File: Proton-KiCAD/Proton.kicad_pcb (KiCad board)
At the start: 4 copper layers, 92.6 x 57.2 mm, 85 parts, among them J1 USB_C_Receptacle_USB2.0_14P, J2 KEYPAD, J3 AudioJack3, J4 SPEAKER_OUT, J5 OLED SPI, J6 ROTARY ENCODER, J7 OLED, J8 SI4703, J9 Conn_01x03_Pin, SW1 BOOTSEL, SW2 RESET, U1 W25Q128JVS, U2 USBLC6-2P6, U3 NCP1117-3.3_SOT223, U4 RP2350_80QFN, U5 TL072, U6 LM386, Y1 ABM8-272-T3

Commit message: ready for final check
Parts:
- added C34: 22uF, Capacitor_SMD:C_0805_2012Metric, B.Cu at (181.5, 56.0)
- added C35: 22uF, Capacitor_SMD:C_0805_2012Metric, B.Cu at (175.2, 56.5)
- added J10: BATTERY IN, Connector_PinHeader_2.54mm:PinHeader_1x02_P2.54mm_Vertical, F.Cu at (180.2, 46.0)
- added J11: FRONT_BUTTON_1, Connector_PinHeader_2.54mm:PinHeader_1x02_P2.54mm_Vertical, F.Cu at (131.8, 64.7)
- added J12: FRONT_BUTTON_2, Connector_PinHeader_2.54mm:PinHeader_1x02_P2.54mm_Vertical, F.Cu at (127.5, 64.7)
- added R31: 1k, Resistor_SMD:R_0402_1005Metric, F.Cu at (135.2, 69.5)
- added R32: 1k, Resistor_SMD:R_0402_1005Metric, F.Cu at (135.2, 67.2)
- added U7: AMS1117-5.0, Package_TO_SOT_SMD:SOT-223-3_TabPin2, B.Cu at (178.8, 50.8)
- C31: moved to B.Cu
- moved C31 5.50 mm to (189.0, 46.0)
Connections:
- U4 pad 11: /GPIO12 -> FRONT_BUTTON_1
- U4 pad 12: /GPIO13 -> FRONT_BUTTON_2
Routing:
- net +5V: track 25.9 -> 41.9 mm, vias 1 -> 2
- net Net-(J10-Pin_1): track 0.00 -> 14.1 mm
- net Net-(J12-Pin_1): track 0.00 -> 9.22 mm
- net Net-(C31-Pad2): track 9.95 -> 15.5 mm
- net FRONT_BUTTON_1: track 0.00 -> 4.96 mm
- net FRONT_BUTTON_2: track 0.00 -> 4.48 mm
- net Net-(J11-Pin_1): track 0.00 -> 4.04 mm
- net Net-(J4-Pin_1): track 6.58 -> 5.83 mm
- net GND: vias 111 -> 130

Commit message: Finished
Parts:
- added J14: DEBUGGER, Connector_PinHeader_2.54mm:PinHeader_1x03_P2.54mm_Vertical, F.Cu at (152.4, 79.5)
- C29: value 0.05 -> 0.05uF
- C3, C5, C6: moved to F.Cu
- C31: value 250uF -> 200uF; footprint Capacitor_THT:CP_Radial_D10.0mm_P5.00mm -> Capacitor_SMD:CP_Elec_6.3x4.5; moved to F.Cu
- J3: value AudioJack3 -> SJ-43514; footprint Connector_Audio:Jack_3.5mm_CUI_SJ-3523-SMT_Horizontal -> Custom_footprints:CUI_SJ-43514
- moved C3 9.34 mm to (145.5, 52.5), turned to 0 degrees
- moved U1 7.32 mm to (141.2, 56.0)
- moved L1 4.63 mm to (148.2, 59.2)
- moved C5 3.62 mm to (148.0, 62.2), turned to 0 degrees
- moved J4 3.10 mm to (184.0, 40.2), turned to 0 degrees
- moved R6 2.93 mm to (148.8, 51.5)
- moved C29 2.50 mm to (177.5, 53.5)
- moved R27 2.49 mm to (177.5, 51.0)
- moved C6 2.06 mm to (148.0, 61.0), turned to 0 degrees
- moved C31 1.27 mm to (190.2, 46.2)
- moved R9 1.00 mm to (146.5, 60.0)
- moved J3 0.69 mm to (200.9, 43.2), turned to -90 degrees
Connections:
- C29 pad 1: GND -> Net-(C29-Pad1)
- C31 pad 2: Net-(C31-Pad2) -> Net-(C29-Pad2)
- R15 pad 1: Net-(J3-PadT) -> Net-(J3-Pad2)
- R27 pad 1: Net-(C31-Pad2) -> Net-(C29-Pad1)
- R27 pad 2: Net-(C29-Pad2) -> GND
- U6 pad 5: Net-(C31-Pad2) -> Net-(C29-Pad2)
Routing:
- net Net-(C29-Pad2): track 1.50 -> 17.4 mm
- net Net-(C31-Pad2): track 15.5 -> 0.00 mm
- net /FLASH_SS: track 13.3 -> 28.0 mm
- net /QSPI_SD0: track 21.8 -> 8.85 mm
- net /SWD: track 0.00 -> 11.7 mm
- net /SWCLK: track 0.00 -> 9.65 mm
- net Net-(J3-Pad2): track 0.00 -> 8.34 mm, vias 0 -> 1
- net /QSPI_SCLK: track 14.6 -> 7.88 mm
- net Net-(J3-PadT): track 4.80 -> 0.00 mm, vias 1 -> 0
- net /QSPI_SD1: track 9.07 -> 13.0 mm
- net /~{USB_BOOT}: track 16.2 -> 13.1 mm
- net /QSPI_SD2: track 7.81 -> 10.1 mm
- net UART_RX: track 26.5 -> 28.5 mm
- net UART_TX: track 23.8 -> 25.7 mm
- net Net-(J4-Pin_1): track 5.83 -> 7.41 mm
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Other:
- board size 92.6 x 57.2 mm -> 92.8 x 57.2 mm
- board text added: "+3.3V"
- board text added: "- TEAM FLYING MACHINE"
- board text added: "FB_1"
- board text added: "FB_2"
- board text added: "GND"
- board text added: "ROTARY ENCODER"
- board text added: "RX"
- board text added: "SPKR"
- board text added: "SWCLK"
- board text added: "SWD"
- board text added: "Si4703"
- board text added: "TX"
- board text added: "{dblquote}SHABANG!{dblquote}"

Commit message: fixed audio section
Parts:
- added C27: 0.1uF, Capacitor_SMD:C_0402_1005Metric, F.Cu at (204.5, 50.1)
- added R33: 1k, Resistor_SMD:R_0402_1005Metric, F.Cu at (188.5, 65.1)
- added R34: 100k, Resistor_SMD:R_0402_1005Metric, F.Cu at (206.2, 54.6)
- turned R26 to 90 degrees
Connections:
- C22 pad 2: GND -> VGND
- C23 pad 1: GND -> VGND
- C23 pad 2: Net-(U5C-V-) -> GND
- C24 pad 2: GND -> VGND
- C30 pad 2: RF_AUDIO -> Net-(C30-Pad2)
- J3 pad 2: Net-(J3-Pad2) -> Net-(C27-Pad1)
- R15 pad 1: Net-(J3-Pad2) -> Net-(C27-Pad2)
- R26 pad 2: GND -> VGND
- R28 pad 2: RF_AUDIO -> Net-(C30-Pad2)
- R29 pad 1: RF_AUDIO -> Net-(C30-Pad2)
- U5 pad 4: Net-(U5C-V-) -> GND
- U6 pad 4: Net-(U6-GND) -> GND
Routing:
- net VGND: track 0.00 -> 44.9 mm, vias 0 -> 5
- net Net-(J3-Pad2): track 8.34 -> 0.00 mm, vias 1 -> 0
- net RF_AUDIO: track 45.7 -> 39.4 mm
- net Net-(C30-Pad2): track 0.00 -> 5.59 mm
- net Net-(C27-Pad2): track 0.00 -> 5.18 mm, vias 0 -> 1
- net Net-(C27-Pad1): track 0.00 -> 3.99 mm
- net Net-(U6-GND): track 3.81 -> 0.00 mm
- net GND: track 6.44 -> 9.70 mm, vias 131 -> 126
- net Net-(U5C-V-): track 3.25 -> 0.00 mm

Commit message: BOM CHANGES
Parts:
- removed the C27 at (174.5, 62.0)
- removed C28: 47uF, Capacitor_SMD:C_0805_2012Metric
- C27: value 0.1uF -> 22nF
- R15, R21: value 1k -> 2k
- R25: value 4k -> 9k
- R34: value 100k -> 2k
- moved C27 16.2 mm to (189.9, 57.1), turned to 0 degrees
- moved R34 15.9 mm to (190.4, 55.9), turned to 0 degrees
- moved C26 1.79 mm to (188.1, 55.9)
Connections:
- C26 pad 1: Net-(U5A--) -> Net-(C26-Pad1)
- C27 pad 1: Net-(C27-Pad1) -> Net-(C26-Pad1)
- C27 pad 2: Net-(C27-Pad2) -> VGND
- J3 pad 2: Net-(C27-Pad1) -> Net-(J3-Pad2)
- R15 pad 1: Net-(C27-Pad2) -> Net-(J3-Pad2)
- R34 pad 1: Net-(C27-Pad2) -> Net-(C26-Pad1)
- R34 pad 2: VGND -> Net-(U5A--)
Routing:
- net Net-(J3-Pad2): track 0.00 -> 8.54 mm
- net Net-(C27-Pad2): track 5.18 -> 0.00 mm, vias 1 -> 0
- net Net-(C27-Pad1): track 3.99 -> 0.00 mm
- net +5V: track 41.9 -> 37.9 mm
- net Net-(C26-Pad1): track 0.00 -> 2.76 mm
- net VGND: track 44.9 -> 45.8 mm
- net GND: vias 126 -> 124
- net /VREG_LX: vias 1 -> 0

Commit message: saving
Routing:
- net VGND: track 45.8 -> 44.9 mm
- net GND: vias 124 -> 134
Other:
- board text added: "- THE FLYING MACHINE"
- board text removed: "- TEAM FLYING MACHINE"
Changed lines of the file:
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@@
 		)
 	)
-	(gr_text "- TEAM FLYING MACHINE\n"
+	(gr_text "- THE FLYING MACHINE\n"
 		(at 191 82.75 0)
 		(layer "F.SilkS")
@@
 	)
 	(via
-		(at 172.5 64)
-		(size 0.6)
-		(drill 0.3)
-		(layers "F.Cu" "B.Cu")
-		(free yes)
-		(net 1)
-	)
-	(via
 		(at 185 50.25)
 		(size 0.6)
@@
 	)
 	(via
-		(at 172.5 63)
-		(size 0.6)
-		(drill 0.3)
-		(layers "F.Cu" "B.Cu")
-		(free yes)
-		(net 1)
-	)
-	(via
 		(at 174.5 38.5)
 		(size 0.6)
@@
 	)
 	(via
-		(at 174 65)
-		(size 0.6)
-		(drill 0.3)
-		(layers "F.Cu" "B.Cu")
-		(free yes)
-		(net 1)
-	)
-	(via
-		(at 176 64.5)
+		(at 175.5 60.65)
 		(size 0.6)
 		(drill 0.3)
@@
 	(via
 		(at 131 82.5)
+		(size 0.6)
+		(drill 0.3)
+		(layers "F.Cu" "B.Cu")
+		(free yes)
+		(net 1)
+	)
+	(via
+		(at 187.25 61.4)
 		(size 0.6)
 		(drill 0.3)
@@
 	)
 	(via
+		(at 197.010702 42.64261)
+		(size 0.6)
+		(drill 0.3)
+		(layers "F.Cu" "B.Cu")
+		(free yes)
+		(net 1)
+	)
+	(via
+		(at 176.25 59.9)
+		(size 0.6)
+		(drill 0.3)
+		(layers "F.Cu" "B.Cu")
+		(free yes)
+		(net 1)
+	)
+	(via
 		(at 171.5 42)
 		(size 0.6)
@@
 	(via
 		(at 169 55.5)
-		(size 0.6)
-		(drill 0.3)
-		(layers "F.Cu" "B.Cu")
-		(free yes)
-		(net 1)
-	)
-	(via
-		(at 172.5 62)
 		(size 0.6)
 		(drill 0.3)
@@
 	)
 	(via
+		(at 196.793598 38.662382)
+		(size 0.6)
+		(drill 0.3)
+		(layers "F.Cu" "B.Cu")
+		(free yes)
+		(net 1)
+	)
+	(via
 		(at 129 81.5)
 		(size 0.6)
@@
 	(via
 		(at 171.5 58)
+		(size 0.6)
+		(drill 0.3)
+		(layers "F.Cu" "B.Cu")
+		(free yes)
+		(net 1)
+	)
+	(via
+		(at 174 60.65)
 		(size 0.6)
 		(drill 0.3)
@@
 	)
 	(via
+		(at 197.851977 42.335047)
+		(size 0.6)
+		(drill 0.3)
+		(layers "F.Cu" "B.Cu")
+		(free yes)
+		(net 1)
+	)
+	(via
 		(at 200 51.5)
 		(size 0.6)
@@
 	)
 	(via
+		(at 195.25 38.4)
+		(size 0.6)
+		(drill 0.3)
+		(layers "F.Cu" "B.Cu")
+		(free yes)
+		(net 1)
+	)
+	(via
 		(at 135.75 57.25)
 		(size 0.5)
@@
 	)
 	(via
+		(at 194.25 39.15)
+		(size 0.6)
+		(drill 0.3)
+		(layers "F.Cu" "B.Cu")
+		(free yes)
+		(net 1)
+	)
+	(via
 		(at 129.5 82)
+		(size 0.6)
+		(drill 0.3)
+		(layers "F.Cu" "B.Cu")
+		(free yes)
+		(net 1)
+	)
+	(via
+		(at 197.589644 38.978991)
 		(size 0.6)
 		(drill 0.3)
@@
 	)
 	(via
-		(at 187 61.5)
+		(at 187.25 63.65)
+		(size 0.6)
+		(drill 0.3)
+		(layers "F.Cu" "B.Cu")
+		(free yes)
+		(net 1)
+	)
+	(via
+		(at 187 62.4)
 		(size 0.6)
 		(drill 0.3)
@@
 	)
 	(via
+		(at 198.20477 40.480623)
+		(size 0.6)
+		(drill 0.3)
+		(layers "F.Cu" "B.Cu")
+		(free yes)
+		(net 1)
+	)
+	(via
 		(at 175.25 46.5)
 		(size 0.6)
@@
 	)
 	(via
+		(at 195.75 42.65)
+		(size 0.6)
+		(drill 0.3)
+		(layers "F.Cu" "B.Cu")
+		(free yes)
+		(net 1)
+	)
+	(via
 		(at 166 41.5)
 		(size 0.6)
@@
 	(via
 		(at 154.5 62.5)
+		(size 0.6)
+		(drill 0.3)
+		(layers "F.Cu" "B.Cu")
+		(free yes)
+		(net 1)
+	)
+	(via
+		(at 194.5 42.4)
 		(size 0.6)
 		(drill 0.3)
@@
 		(net 1)
 	)
+	(via
+		(at 198.494241 41.367128)
+		(size 0.6)
+		(drill 0.3)
+		(layers "F.Cu" "B.Cu")
+		(free yes)
+		(net 1)
+	)
 	(segment
 		(start 144.77 71.39)
@@
 		(start 196.4581 66.848522)
 		(end 196.101478 66.848522)
-		(width 0.254)
+		(width 0.3048)
 		(layer "F.Cu")
 		(net 8)
@@
 		(start 196.101478 66.848522)
 		(end 194.95 68)
-		(width 0.254)
+		(width 0.3048)
 		(layer "F.Cu")
 		(net 8)
@@
 	)
 	(via
-		(at 206.2081 56.098522)
+		(at 205.25 56.65)
 		(size 0.5)
 		(drill 0.4)
@@
 	)
 	(segment
-		(start 204.7081 56.098522)
-		(end 206.2081 56.098522)
-		(width 0.254)
-		(layer "In2.Cu")
-		(net 8)
-	)
-	(segment
 		(start 200.413368 62.848)
 		(end 201.251523 62.848)
@@
 	)
 	(segment
+		(start 204.739416 61.078)
+		(end 202.687578 61.078)
+		(width 0.254)
+		(layer "In2.Cu")
+		(net 8)
+	)
+	(segment
 		(start 206.2081 59.609316)
-		(end 206.2081 56.098522)
+		(end 204.739416 61.078)
 		(width 0.254)
 		(layer "In2.Cu")
@@
 	)
 	(segment
-		(start 200.7081 52.098522)
-		(end 204.7081 56.098522)
-		(width 0.254)
-		(layer "In2.Cu")
-		(net 8)
-	)
-	(segment
-		(start 199.2081 52.098522)
-		(end 200.7081 52.098522)
+		(start 205.25 56.65)
+		(end 204.7081 56.1081)
 		(width 0.254)
 		(layer "In2.Cu")
@@
 	)
 	(segment
-		(start 204.739416 61.078)
-		(end 206.2081 59.609316)
-		(width 0.254)
-		(layer "In2.Cu")
-		(net 8)
-	)
-	(segment
-		(start 202.687578 61.078)
-		(end 204.739416 61.078)
-		(width 0.254)
-		(layer "In2.Cu")
-		(net 8)
-	)
-	(segment
 		(start 189.2081 61.857623)
 		(end 189.2081 58.598522)
@@
 	)
 	(segment
+		(start 205.25 56.65)
+		(end 206.2081 57.6081)
+		(width 0.254)
+		(layer "In2.Cu")
+		(net 8)
+	)
+	(segment
+		(start 202.687578 61.078)
+		(end 202.4581 60.848522)
+		(width 0.254)
+		(layer "In2.Cu")
+		(net 8)
+	)
+	(segment
 		(start 196.4581 66.848522)
 		(end 194.198999 66.848522)
@@
 	)
 	(segment
+		(start 200.7081 52.098522)
+		(end 199.2081 52.098522)
+		(width 0.254)
+		(layer "In2.Cu")
+		(net 8)
+	)
+	(segment
+		(start 204.7081 56.1081)
+		(end 204.7081 56.098522)
+		(width 0.254)
+		(layer "In2.Cu")
+		(net 8)
+	)
+	(segment
 		(start 194.198999 66.848522)
 		(end 189.2081 61.857623)
@@
 	)
 	(segment
-		(start 202.4581 60.848522)
-		(end 202.687578 61.078)
+		(start 204.7081 56.098522)
+		(end 200.7081 52.098522)
 		(width 0.254)
 		(layer "In2.Cu")
+		(net 8)
+	)
+	(segment
+		(start 206.2081 57.6081)
+		(end 206.2081 59.609316)
+		(width 0.254)
+		(layer "In2.Cu")

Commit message: finished updated layout
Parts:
- removed the C22 at (194.0, 68.0)
- removed the C23 at (200.0, 53.5)
- removed the J3 at (200.9, 43.2)
- removed the J4 at (184.0, 40.2)
- removed the R15 at (204.5, 54.5)
- removed the R25 at (191.0, 60.0)
- removed the R26 at (188.5, 60.0)
- removed the U5 at (200.8, 64.3)
- added C28: 22nF, Capacitor_SMD:C_0402_1005Metric, F.Cu at (189.2, 54.4)
- added C32: 22nF, Capacitor_SMD:C_0402_1005Metric, F.Cu at (187.5, 64.4)
- added C33: 1uF, Capacitor_SMD:C_0402_1005Metric, F.Cu at (184.5, 66.7)
- added C34: 0.05uF, Capacitor_SMD:C_0402_1005Metric, F.Cu at (194.2, 48.4)
- added C35: 200uF, Capacitor_SMD:CP_Elec_6.3x4.5, F.Cu at (190.0, 46.1)
- added J12: SPEAKER_OUT, Connector_PinHeader_2.54mm:PinHeader_1x02_P2.54mm_Vertical, F.Cu at (184.0, 40.1)
- added J6: SJ-43514, Custom Footprints:CUI_SJ-43514, B.Cu at (200.9, 43.2)
- added R19: 100k, Resistor_SMD:R_0402_1005Metric, F.Cu at (189.2, 60.4)
- added R20: 100k, Resistor_SMD:R_0402_1005Metric, F.Cu at (187.2, 61.6)
- added R22: 100k, Resistor_SMD:R_0402_1005Metric, F.Cu at (202.0, 60.9)
- added R30: 2k, Resistor_SMD:R_0402_1005Metric, F.Cu at (202.0, 65.2)
- added R31: 2k, Resistor_SMD:R_0402_1005Metric, F.Cu at (189.2, 56.9)
- added R32: 2k, Resistor_SMD:R_0402_1005Metric, F.Cu at (204.8, 62.6)
- added R35: 2k, Resistor_SMD:R_0402_1005Metric, F.Cu at (187.5, 66.4)
- added R38: 10, Resistor_SMD:R_0402_1005Metric, F.Cu at (194.8, 50.1)
- added U7: LM386, Package_DIP:DIP-8_W7.62mm, F.Cu at (185.3, 64.3)
- C24, C25: value 22nF -> 0.1uF
- C26: value 1uF -> 10uF; footprint Capacitor_SMD:C_0402_1005Metric -> Capacitor_SMD:C_0805_2012Metric
- C29: value 0.05uF -> 22nF
- C30: value 0.1uF -> 22nF
- C31: value 200uF -> 22nF; footprint Capacitor_SMD:CP_Elec_6.3x4.5 -> Capacitor_SMD:C_0402_1005Metric
- R21: value 2k -> 100k
- R27: value 10 -> 9k
- R28: value 100k -> 1k
- R29: value 100k -> 2k
- R33: value 1k -> 2k
- U6: value LM386 -> LM324; footprint Package_DIP:DIP-8_W7.62mm -> Package_DIP:DIP-14_W7.62mm
- moved R27 29.2 mm to (202.0, 66.9), turned to 0 degrees
- moved C29 25.3 mm to (202.0, 59.6), turned to 180 degrees
- moved C31 23.6 mm to (187.0, 69.7)
- moved C26 16.4 mm to (195.2, 70.7)
- moved R33 15.6 mm to (202.0, 57.4), turned to 180 degrees
- moved U6 13.2 mm to (191.7, 52.8), turned to 0 degrees
- moved C30 13.1 mm to (201.8, 55.1), turned to 180 degrees
- moved R34 12.4 mm to (187.5, 67.9)
- moved C25 10.3 mm to (201.8, 50.6)
- moved C24 9.00 mm to (204.5, 50.6)
- moved R28 8.80 mm to (197.8, 70.7), turned to -90 degrees
- moved R21 6.09 mm to (202.0, 62.9), turned to 180 degrees
- moved R29 5.90 mm to (187.8, 56.6)
- moved C27 2.03 mm to (188.5, 58.6), turned to 180 degrees
- renumbered C8 to C10, C9 to C11, C10 to C12, C11 to C13, C12 to C14, C13 to C15, C14 to C16, C15 to C17, C16 to C18, C17 to C19, C18 to C20, C19 to C21, C20 to C22, C21 to C23, C34 to C3, C32 to C36, C33 to C37, C3 to C4, C35 to C5, C4 to C6, C5 to C7, C6 to C8, C7 to C9, J10 to J1, J11 to J10, J5 to J11, J8 to J13, J1 to J2, J14 to J3, J9 to J4, J2 to J5, J6 to J7, J7 to J8, J12 to J9, R16 to R15, R17 to R16, R18 to R17, R19 to R18, R20 to R23, R22 to R24, R23 to R25, R24 to R26, R32 to R36, R31 to R37, R30 to R39, U7 to U1, U1 to U2, U2 to U3, U3 to U4, U4 to U5
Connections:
- C24 pad 1: Net-(U5A-+) -> Net-(C24-Pad1)
- C24 pad 2: VGND -> Net-(U6B-+)
- C25 pad 2: Net-(U5A--) -> Net-(U6C-+)
- C26 pad 2: Net-(U6-+) -> GND
- C27 pad 1: Net-(C26-Pad1) -> Net-(U6A-+)
- C27 pad 2: VGND -> GND
- C29 pad 1: Net-(C29-Pad1) -> Net-(U6D-+)
- C29 pad 2: Net-(C29-Pad2) -> GND
- C30 pad 2: Net-(C30-Pad2) -> Net-(U6D--)
- C31 pad 1: Net-(J4-Pin_1) -> RF_AUDIO
- C31 pad 2: Net-(C29-Pad2) -> GND
- R21 pad 1: Net-(C25-Pad1) -> +3.3V
- R21 pad 2: Net-(U5A-+) -> Net-(U6C-+)
- R27 pad 1: Net-(C29-Pad1) -> Net-(U6C--)
- R27 pad 2: GND -> Net-(R27-Pad2)
- R28 pad 1: +3.3V -> Net-(U6C--)
- R28 pad 2: Net-(C30-Pad2) -> Net-(C26-Pad1)
- R29 pad 1: Net-(C30-Pad2) -> Net-(U6B--)
- R29 pad 2: GND -> Net-(C28-Pad1)
- R33 pad 1: Net-(C30-Pad2) -> Net-(C30-Pad1)
- R33 pad 2: RF_AUDIO -> Net-(U6D-+)
- R34 pad 1: Net-(C26-Pad1) -> RF_AUDIO
- R34 pad 2: Net-(U5A--) -> Net-(U6A--)
- U5 pad 53: /GPIO42_ADC2 -> RF_AUDIO_2
- U6 pad 1: unconnected-(U6-GAIN-Pad1) -> Net-(U6A--)
- U6 pad 2: GND -> Net-(U6A--)
- U6 pad 3: Net-(U6-+) -> Net-(U6A-+)
- U6 pad 4: GND -> +3.3V
- U6 pad 5: Net-(C29-Pad2) -> Net-(U6B-+)
- U6 pad 6: +5V -> Net-(U6B--)
- U6 pad 7: unconnected-(U6-BYPASS-Pad7) -> Net-(U6B--)
- U6 pad 8: unconnected-(U6-GAIN-Pad8) -> Net-(R27-Pad2)
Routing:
- net VGND: track 44.9 -> 0.00 mm, vias 5 -> 0
- net RF_AUDIO_2: track 0.00 -> 39.5 mm
- net Net-(U6B-+): track 0.00 -> 23.5 mm, vias 0 -> 1
- net Net-(U6A--): track 0.00 -> 22.2 mm, vias 0 -> 2
- net Net-(C34-Pad2): track 0.00 -> 22.0 mm
- net Net-(U6D--): track 0.00 -> 21.4 mm
- net Net-(U5A--): track 21.1 -> 0.00 mm
- net Net-(C29-Pad2): track 17.4 -> 0.00 mm
- net Net-(U6C-+): track 0.00 -> 15.3 mm, vias 0 -> 2
- net Net-(U6B--): track 0.00 -> 13.1 mm, vias 0 -> 1
- net Net-(U7-+): track 0.00 -> 8.57 mm
- net Net-(J3-Pad2): track 8.54 -> 0.00 mm
- net Net-(R27-Pad2): track 0.00 -> 8.47 mm
- net Net-(U6C--): track 0.00 -> 8.07 mm
- net Net-(J4-Pin_1): track 7.41 -> 0.00 mm
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
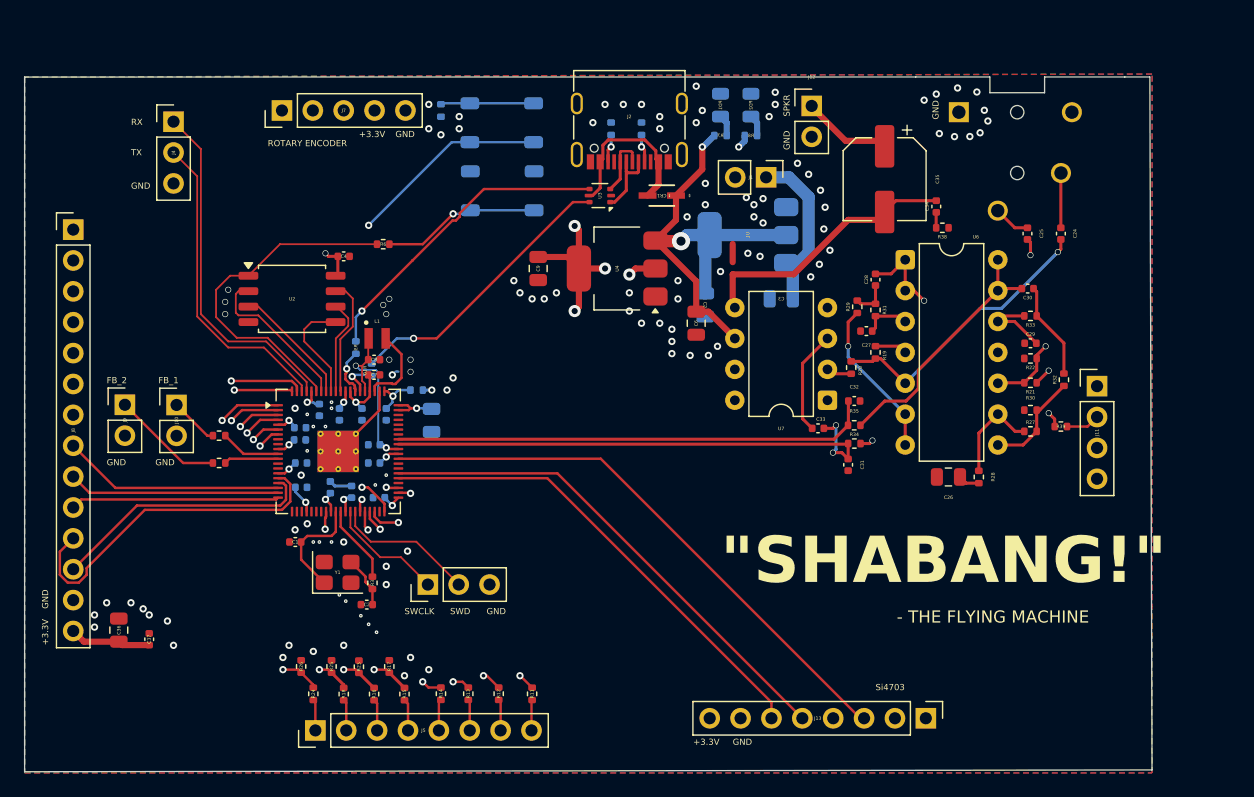
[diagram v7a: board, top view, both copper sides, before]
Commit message: BOM and CPL changes
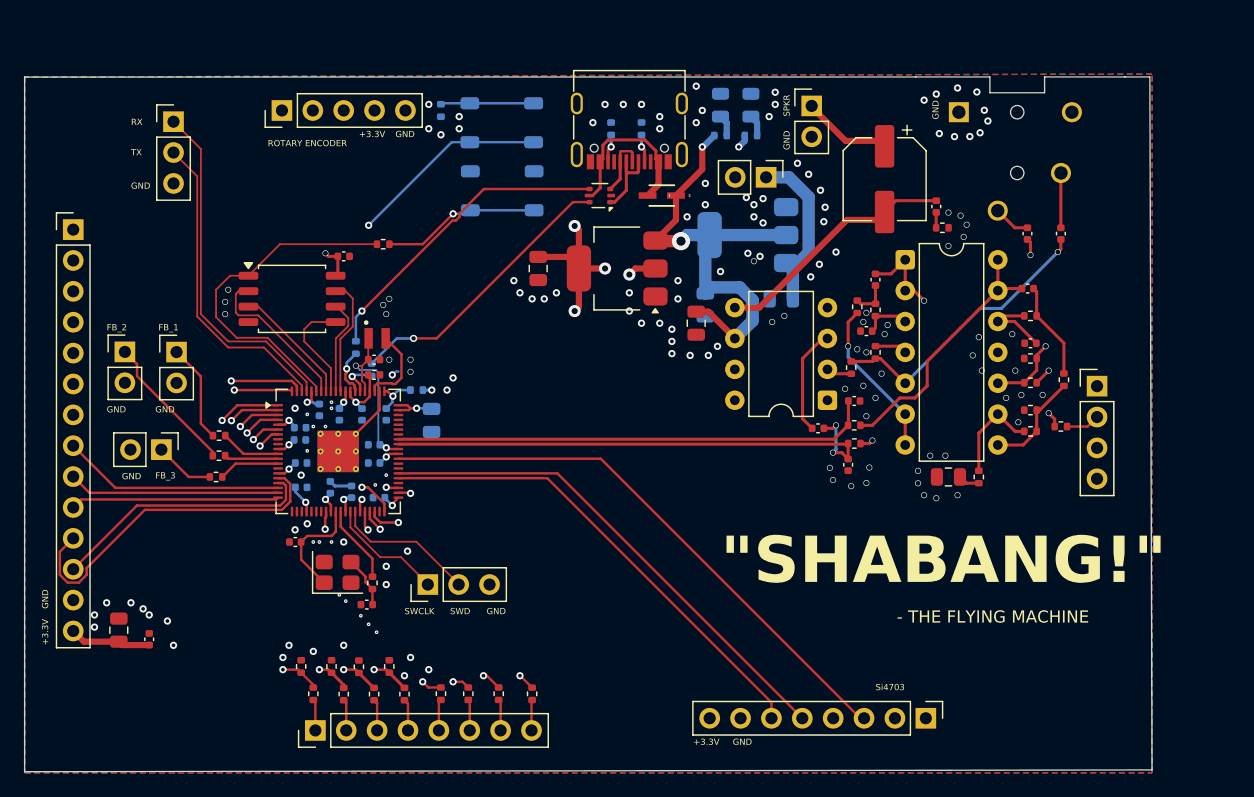
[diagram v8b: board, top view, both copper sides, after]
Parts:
- added J14: FRONT_BUTTON_3, Connector_PinHeader_2.54mm:PinHeader_1x02_P2.54mm_Vertical, F.Cu at (130.5, 68.4)
- added R40: 1k, Resistor_SMD:R_0402_1005Metric, F.Cu at (135.0, 70.7)
- moved J10 4.35 mm to (131.8, 60.4)
- moved J9 4.35 mm to (127.5, 60.4)
- moved R37 0.60 mm to (135.2, 68.9)
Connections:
- U5 pad 13: /GPIO14 -> FRONT_BUTTON_3
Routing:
- net FRONT_BUTTON_3: track 0.00 -> 5.05 mm
- net Net-(J14-Pin_1): track 0.00 -> 4.92 mm
- net Net-(J10-Pin_1): track 4.04 -> 8.11 mm
- net Net-(J9-Pin_1): track 9.22 -> 11.5 mm
- net Net-(C34-Pad2): track 22.0 -> 20.5 mm
- net (no net): track 1.50 -> 0.00 mm
- net +5V: track 37.9 -> 39.0 mm
- net GND: vias 114 -> 154
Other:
- board text added: "FB_3"
